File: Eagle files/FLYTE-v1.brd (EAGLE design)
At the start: 160 x 100 mm, 42 parts, among them J2 CONSMA002, Q1 IRF540NPBF, Q2 IRF540NPBF, SW1 1825159-1, U2 AMS1117-3.3, U3 CORE1262-868M, U6 W25Q32JVSSIQ

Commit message: Finish v1 schematic
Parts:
- added U$4: NEO-6M, NEO-6M:NEO-6M
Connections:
- net 3V3: now also U$4.VCC
- net GND: now also U$4.GND
- net RX: now also U$4.TX
- net TX: now also U$4.RX
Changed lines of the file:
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@@
 <attribute name="VALUE" x="-99.06" y="-76.835" size="0.6096" layer="27" font="vector" ratio="20" align="top-center"/>
 </element>
+<element name="U$4" library="NEO-6M" package="NEO-6M" override_package3d_urn="urn:adsk.eagle:package:40381906/2" override_package_urn="urn:adsk.eagle:footprint:40381907/1" value="NEO-6M" x="-134.62" y="-76.2" smashed="yes"/>
 </elements>
 <signals>
@@
 <contactref element="SW1" pad="1"/>
 <contactref element="S1" pad="3"/>
+<contactref element="U$4" pad="GND"/>
+<wire x1="-102.3112" y1="-75.9206" x2="-125.73" y2="-74.93" width="0" layer="19" extent="1-1"/>
 <wire x1="-102.55" y1="-59.69" x2="-102.3112" y2="-75.9206" width="0" layer="19" extent="1-1"/>
 <wire x1="-97.75" y1="-50.8" x2="-102.55" y2="-59.69" width="0" layer="19" extent="1-1"/>
@@
 <contactref element="R17" pad="1"/>
 <contactref element="SW1" pad="3"/>
+<contactref element="U$4" pad="VCC"/>
+<wire x1="-92.75" y1="-50.8" x2="-118.11" y2="-74.93" width="0" layer="19" extent="1-1"/>
+<wire x1="-102.55" y1="-41.91" x2="-92.75" y2="-50.8" width="0" layer="19" extent="1-1"/>
 <wire x1="-100.65" y1="-35.56" x2="-102.55" y2="-41.91" width="0" layer="19" extent="1-1"/>
 <wire x1="-102.55" y1="-29.21" x2="-100.65" y2="-35.56" width="0" layer="19" extent="1-1"/>
@@
 <wire x1="-95.46" y1="5.715" x2="-102.66" y2="4.445" width="0" layer="19" extent="1-1"/>
 <wire x1="-95.46" y1="6.985" x2="-95.46" y2="5.715" width="0" layer="19" extent="1-1"/>
-<wire x1="-92.75" y1="-50.8" x2="-102.55" y2="-41.91" width="0" layer="19" extent="1-1"/>
 <wire x1="-75.2" y1="25.27" x2="-95.46" y2="6.985" width="0" layer="19" extent="1-1"/>
 <wire x1="-57.83" y1="5.08" x2="-75.2" y2="25.27" width="0" layer="19" extent="1-1"/>
@@
 <signal name="TX">
 <contactref element="U1" pad="P$1"/>
+<contactref element="U$4" pad="RX"/>
+<wire x1="-35.4" y1="53.34" x2="-120.65" y2="-74.93" width="0" layer="19" extent="1-1"/>
 </signal>
 <signal name="RX">
 <contactref element="U1" pad="P$2"/>
+<contactref element="U$4" pad="TX"/>
+<wire x1="-35.4" y1="50.8" x2="-123.19" y2="-74.93" width="0" layer="19" extent="1-1"/>
 </signal>
 <signal name="N$2">

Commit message: Finish layout
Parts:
- removed R2: 470ohm, rcl:R0805
- added C3, C4: 22uF, SparkFun-Capacitors:0805
- added JP1, JP2, JP3, JP4: (no value), adafruit:1X03
- added U$5, U$6, U$7, U$8: (no value), holes:3,0
- added U4: AMS1117-3.3, AMS1117-3.3:SOT229P700X180-4N
- moved U$4 209.0 mm to (32.0, 50.0), turned to 270 degrees
- moved DROGUE-VCC 206.5 mm to (115.0, 40.0)
- moved R9 201.3 mm to (104.0, 35.0), turned to 90 degrees
- moved DROGUE-GND 199.8 mm to (115.0, 31.0)
- moved R4 185.0 mm to (70.0, 40.0), flipped to the bottom, turned to 90 degrees
- moved R3 184.5 mm to (70.0, 45.0), flipped to the bottom, turned to 270 degrees
- moved C2 182.7 mm to (92.0, 32.0), flipped to the bottom, turned to 180 degrees
- moved C1 178.9 mm to (90.0, 29.0), flipped to the bottom, turned to 270 degrees
- moved DR_ARM_IN 178.1 mm to (103.0, 52.0)
- moved U2 176.0 mm to (96.0, 27.0), flipped to the bottom, turned to 90 degrees
- moved R17 174.8 mm to (64.0, 14.0), flipped to the bottom
- moved S1 172.9 mm to (26.1, 45.7), turned to 180 degrees
- moved R15 169.5 mm to (63.6, 21.5), flipped to the bottom
- moved LS1 168.2 mm to (79.0, 39.0)
- moved R14 166.9 mm to (64.0, 11.0), flipped to the bottom
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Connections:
- removed net N$2: LS1.-, R2.1
- new net 5V: C3.2, JP1.2, JP2.2, JP3.2, JP4.2, U4.2
- new net SERVO1: JP1.1, U1.P$6
- new net SERVO2: JP2.1, U1.P$7
- new net SERVO3: JP3.1, U1.P$10
- new net SERVO4: JP4.1, U1.P$11
- net BUZZER: now also LS1.-; no longer R2.2
- net GND: now also C3.1, C4.1, JP1.3, JP2.3, JP3.3, JP4.3, U4.1
- net VCC: now also C4.2, U4.3
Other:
- board size 160 x 100 mm -> 120 x 55 mm

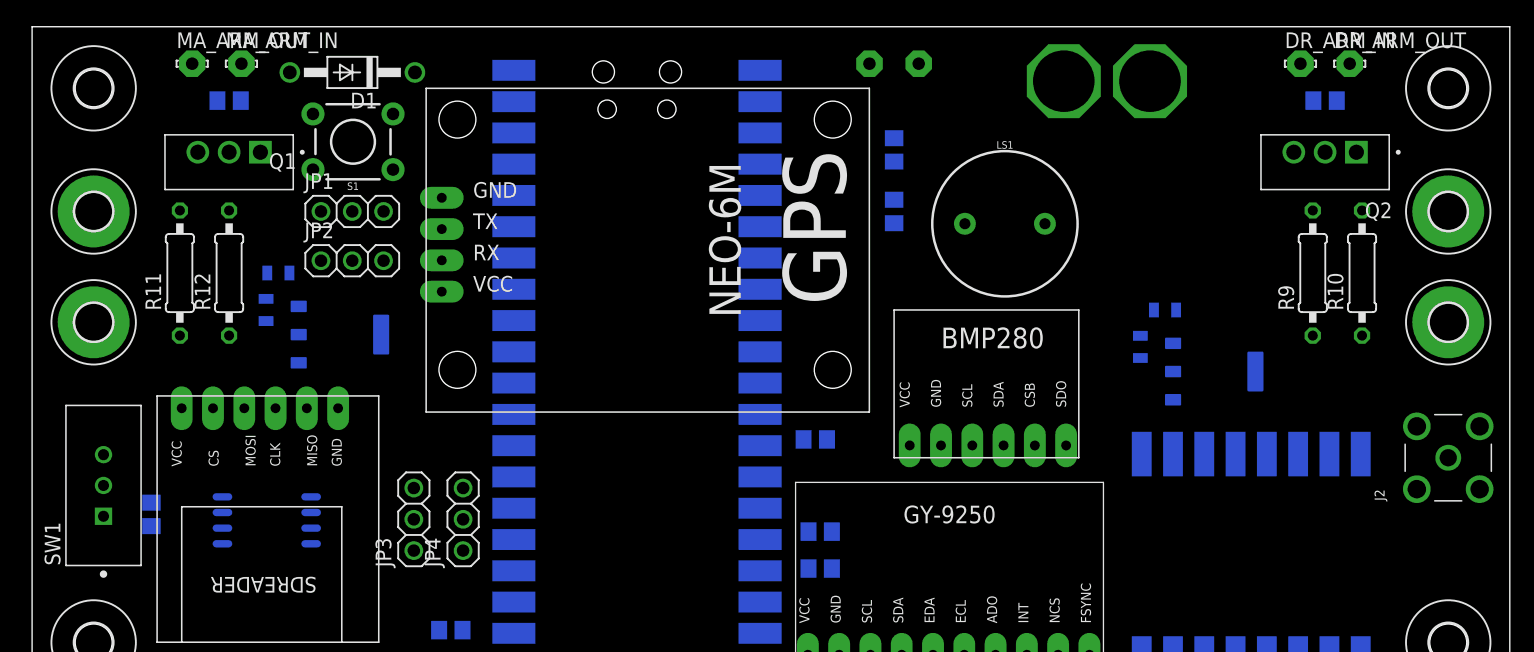
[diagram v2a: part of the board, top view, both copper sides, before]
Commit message: Finish layout with GPS
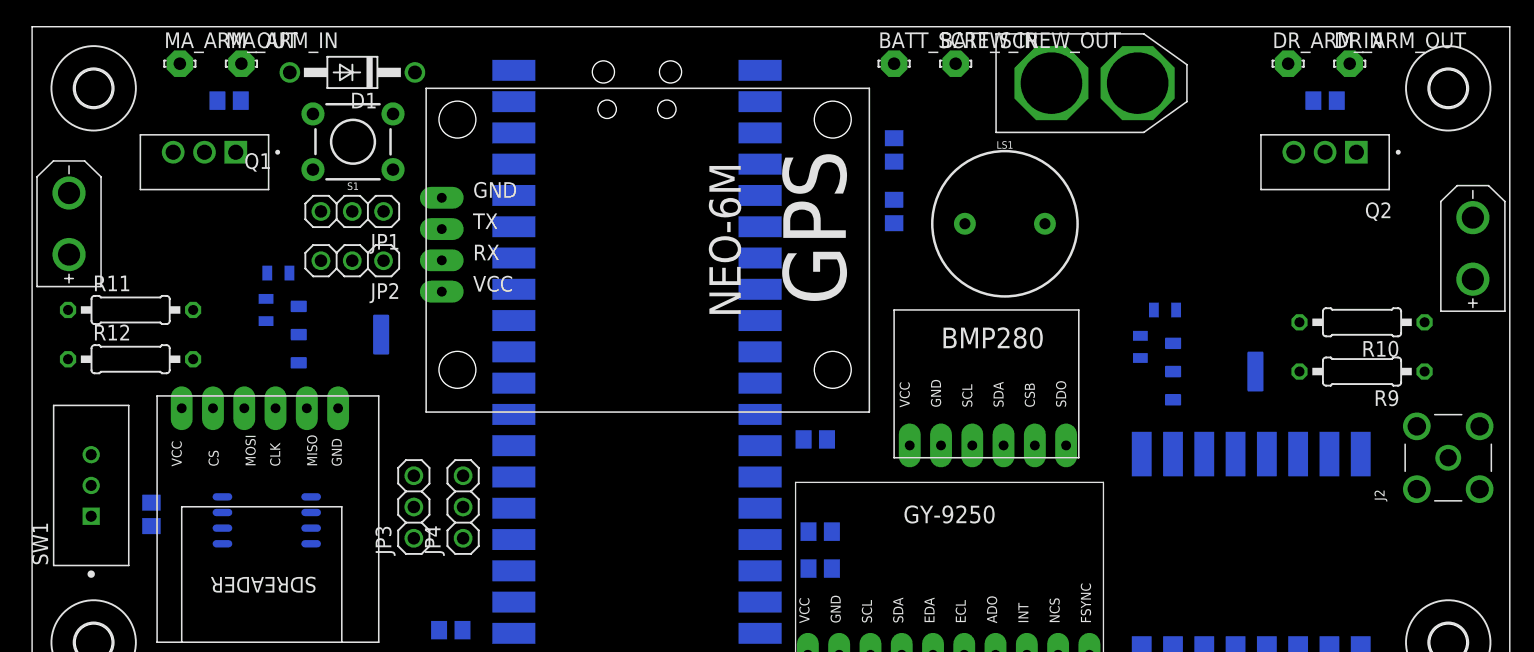
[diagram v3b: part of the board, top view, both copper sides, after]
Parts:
- removed DROGUE-GND, DROGUE-VCC, MAIN-GND, MAIN-VCC: MOUNT-PAD-ROUND3.0, holes:3,0-PAD
- added DROGUE_IN, MAIN_IN: XT30UPB-M, XT30UPB-M:XT30UPB-M
- moved R12 10.6 mm to (8.00, 28.0), turned to 0 degrees
- moved R9 8.94 mm to (108.0, 27.0), turned to 180 degrees
- moved R11 5.00 mm to (8.00, 32.0), turned to 0 degrees
- moved R10 4.00 mm to (108.0, 31.0), turned to 180 degrees
- moved BATT_SCREW_OUT 3.00 mm to (75.0, 52.0), flipped to the top
- moved BATT_SCREW_IN 2.00 mm to (70.0, 52.0), flipped to the top
- moved Q1 2.00 mm to (14.0, 44.0)
- moved BATT_IN 1.01 mm to (78.3, 50.4), flipped to the top, turned to 0 degrees
- moved DR_ARM_IN 1.00 mm to (102.0, 52.0)
- moved JP3 1.00 mm to (31.0, 16.0)
- moved JP4 1.00 mm to (35.0, 16.0)
- moved MA_ARM_OUT 1.00 mm to (12.0, 52.0)
- moved SW1 1.00 mm to (4.80, 17.8)
- turned JP1 to 180 degrees
- turned JP2 to 180 degrees
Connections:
- removed net N$5: DROGUE-VCC.B3,0, DR_ARM_OUT.MP
- new net N$2: DROGUE_IN.P$2, DR_ARM_OUT.MP
- net N$14: now also MAIN_IN.P$2; no longer MAIN-VCC.B3,0
- net N$6: now also MAIN_IN.P$1; no longer MAIN-GND.B3,0
- net N$7: now also DROGUE_IN.P$1; no longer DROGUE-GND.B3,0

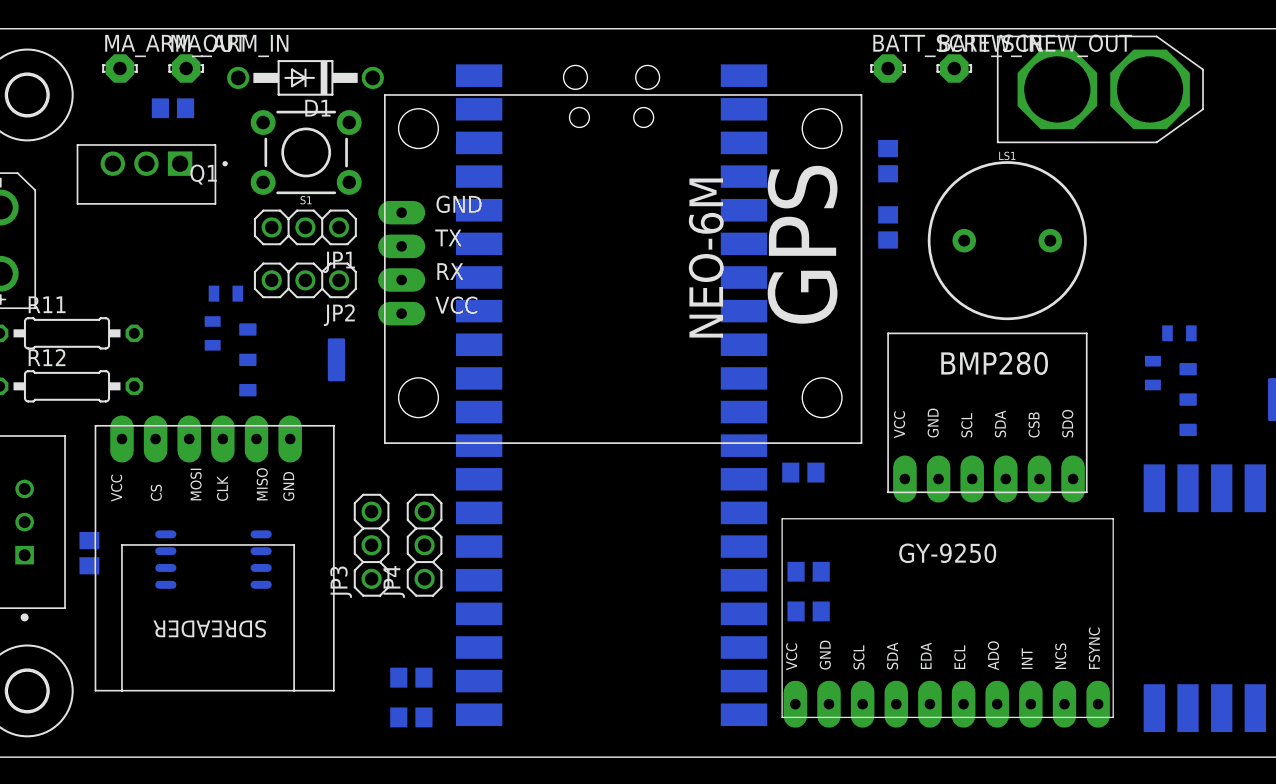
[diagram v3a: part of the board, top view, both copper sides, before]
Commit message: move resistors, remove 1 screw sw
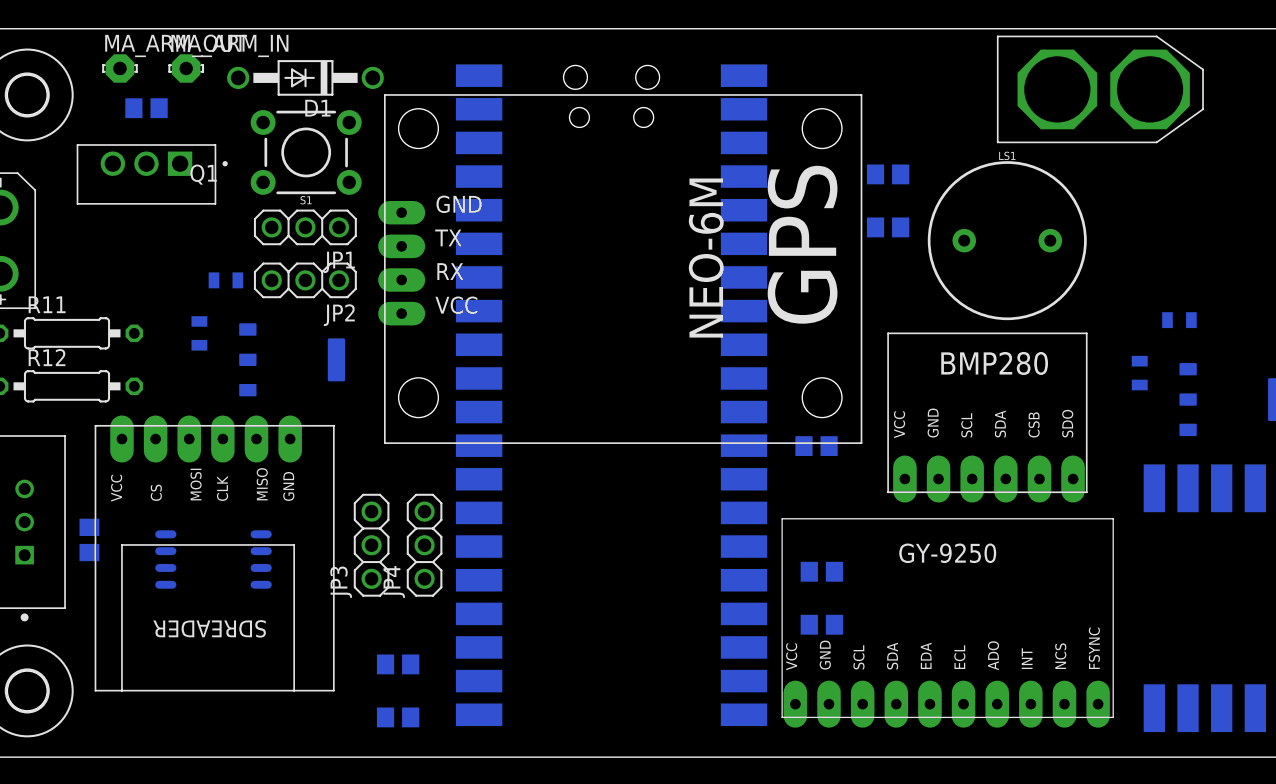
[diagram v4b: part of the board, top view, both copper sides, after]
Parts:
- removed BATT_SCREW_IN, BATT_SCREW_OUT: LSP10, solpad:LSP10
- moved R15 2.24 mm to (64.6, 23.5)
- moved R8 2.00 mm to (14.0, 49.0)
- moved R13 1.41 mm to (33.0, 7.00)
- moved R14 1.41 mm to (65.0, 10.0)
- moved C1 1.00 mm to (89.0, 29.0)
- moved C2 1.00 mm to (92.0, 33.0)
- moved C3 1.00 mm to (18.0, 32.0)
- moved C4 1.00 mm to (20.0, 36.0)
- moved R16 1.00 mm to (33.0, 3.00)
- moved R17 1.00 mm to (65.0, 14.0)
- moved R3 1.00 mm to (70.0, 44.0), turned to 0 degrees
- moved R18 1.00 mm to (9.69, 16.4)
- turned R4 to 0 degrees
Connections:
- removed net N$3: BATT_IN.+, BATT_SCREW_OUT.MP
- net VCC: now also BATT_IN.+; no longer BATT_SCREW_IN.MP

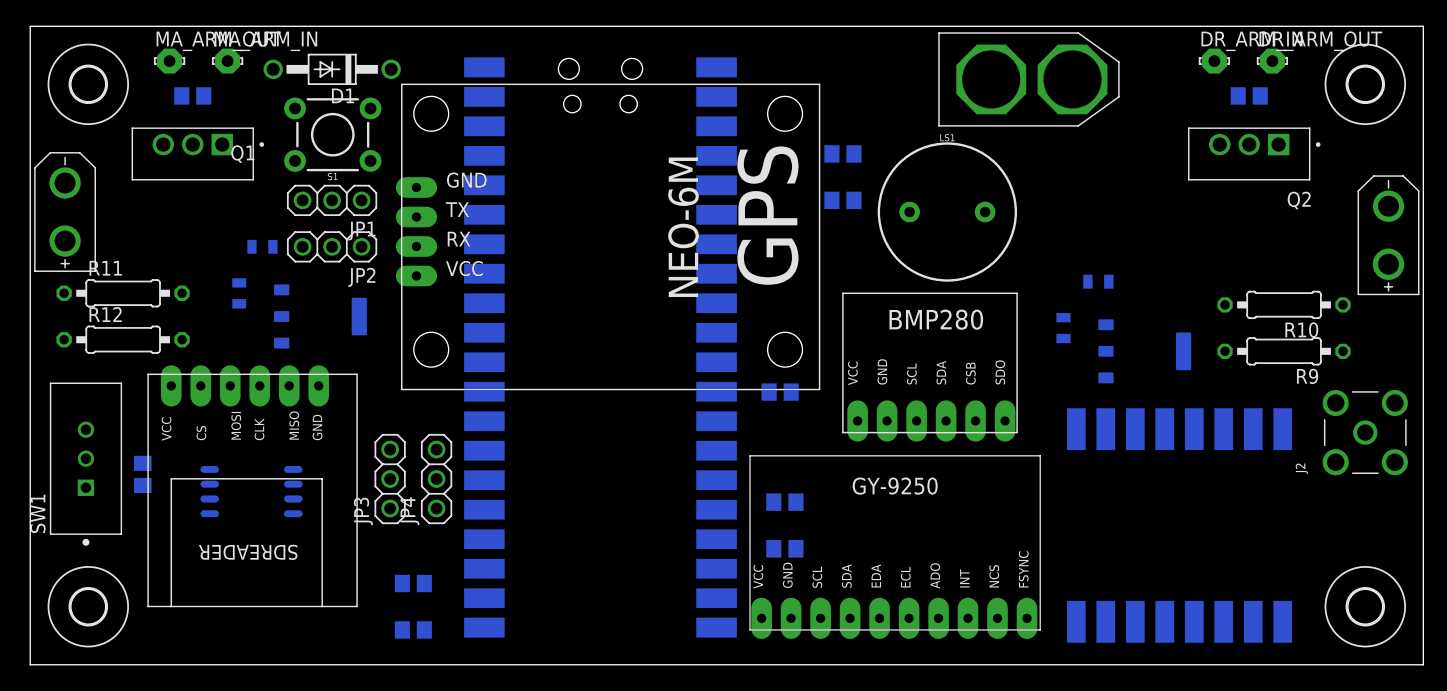
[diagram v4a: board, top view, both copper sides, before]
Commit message: Finish wiring and top layout
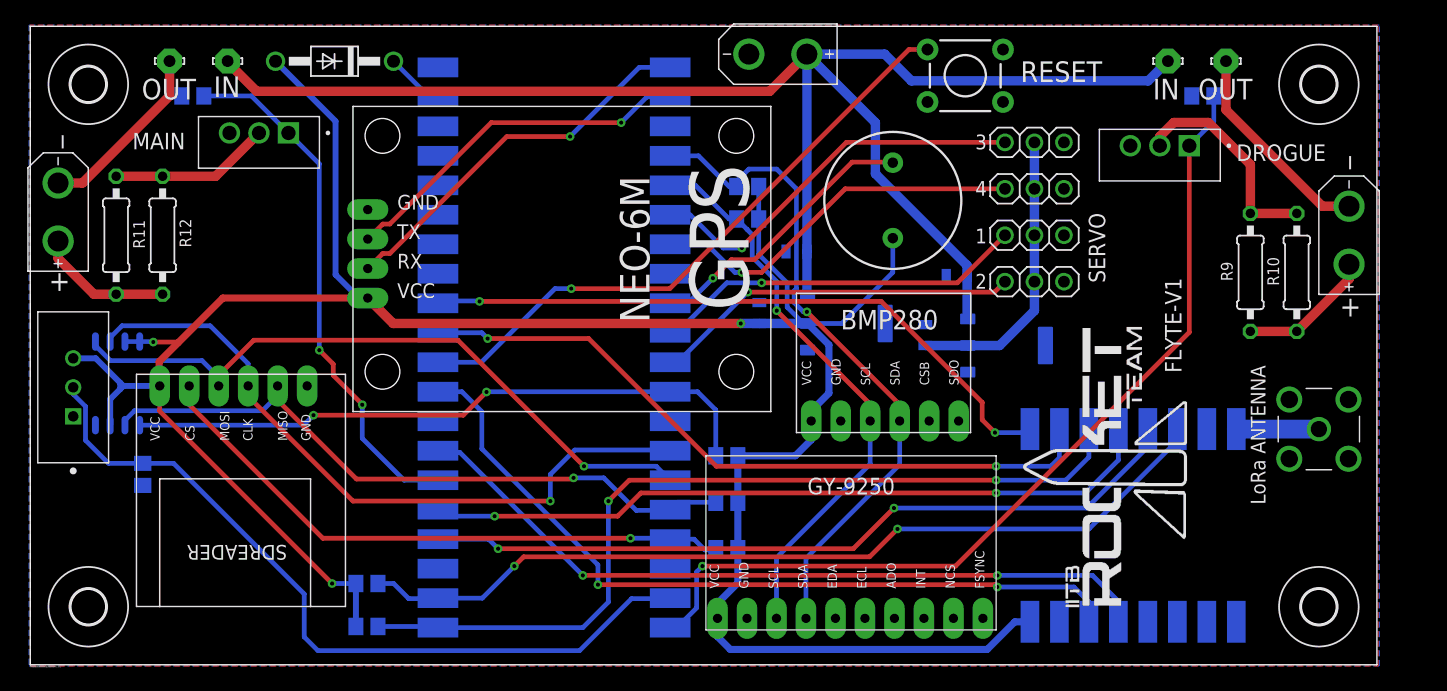
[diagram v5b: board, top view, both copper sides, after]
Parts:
- removed BATT_IN: XT60, XT60:XT60
- removed U2, U4: AMS1117-3.3, AMS1117-3.3:SOT229P700X180-4N
- added 3.3V_REGULATOR, 5V_REGULATOR: AMS1117-3.3, AMS1117-3.3:SOT229P700X180-4N
- added BATTERY: XT30UPB-M, XT30UPB-M:XT30UPB-M
- moved JP3 62.6 mm to (86.5, 45.0), turned to 0 degrees
- moved JP1 60.6 mm to (86.5, 37.0), turned to 0 degrees
- moved JP2 60.6 mm to (86.5, 33.0), turned to 0 degrees
- moved C4 59.9 mm to (79.8, 33.5)
- moved C3 59.2 mm to (77.1, 28.4)
- moved JP4 57.2 mm to (86.5, 41.0), turned to 0 degrees
- moved S1 54.7 mm to (80.5, 50.7), turned to 0 degrees
- moved C1 26.2 mm to (62.8, 30.3)
- moved C2 26.1 mm to (66.0, 35.6)
- moved U6 14.8 mm to (7.52, 24.2), turned to 90 degrees
- moved R12 9.62 mm to (11.4, 37.0), turned to 90 degrees
- moved R3 8.66 mm to (61.8, 41.2)
- moved R4 8.35 mm to (61.8, 38.4)
- moved Q2 7.70 mm to (97.3, 43.9)
- moved R9 7.39 mm to (105.1, 33.8), turned to 90 degrees
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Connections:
- net N$4 renamed ANT
- net 3V3: now also 3.3V_REGULATOR.2, D1.A; no longer U2.2
- net 5V: now also 5V_REGULATOR.2; no longer U4.2
- net BUZZER: now also U1.P$9; no longer U1.P$26
- net GND: now also 3.3V_REGULATOR.1, 5V_REGULATOR.1, BATTERY.P$2; no longer BATT_IN.-, U2.1, U4.1
- net MAIN: now also U1.P$26; no longer U1.P$19
- net PROG: now also U1.P$19; no longer U1.P$9
- net SERVO1: now also U1.P$10; no longer U1.P$6
- net SERVO2: now also U1.P$11; no longer U1.P$7
- net SERVO3: now also U1.P$6; no longer U1.P$10
- net SERVO4: now also U1.P$7; no longer U1.P$11
- net VCC: now also 3.3V_REGULATOR.3, 5V_REGULATOR.3, BATTERY.P$1; no longer BATT_IN.+, D1.A, U2.3, U4.3
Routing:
- net 3V3: track 0.00 -> 220.5 mm, vias 0 -> 3
- net VCC: track 0.00 -> 134.6 mm
- net DROGUE: track 0.00 -> 78.3 mm, vias 0 -> 1
- net CS_SX: track 0.00 -> 76.0 mm, vias 0 -> 2
- net MISO_0: track 0.00 -> 74.9 mm, vias 0 -> 2
- net SX_DIO1: track 0.00 -> 68.2 mm, vias 0 -> 2
- net PROG: track 0.00 -> 67.9 mm
- net SCK_0: track 0.00 -> 66.7 mm, vias 0 -> 2
- net SX_DIO2: track 0.00 -> 65.8 mm, vias 0 -> 2
- net MOSI_0: track 0.00 -> 63.5 mm, vias 0 -> 2
- net SX_RESET: track 0.00 -> 61.1 mm, vias 0 -> 2
- net SCK_1: track 0.00 -> 60.1 mm, vias 0 -> 1
- net MOSI_1: track 0.00 -> 58.9 mm, vias 0 -> 1
- net MISO_1: track 0.00 -> 58.6 mm, vias 0 -> 1
- net SDA: track 0.00 -> 57.9 mm, vias 0 -> 1
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- added copper zone on layer 1, net GND
- added copper zone on layer 16, net GND
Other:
- board size 120 x 55 mm -> 116 x 55 mm
- board text added: "+"
- board text added: "1"
- board text added: "2"
- board text added: "3"
- board text added: "4"
- board text added: "C:/Users/shobh/Downloads/logo_board (1).bmp"
- board text added: "DROGUE"
- board text added: "FLYTE-V1"
- board text added: "IN"
- board text added: "LoRa ANTENNA"
- board text added: "MAIN"
- board text added: "OUT"
- board text added: "RESET"
- board text added: "SERVO"
- board text added: "_"
